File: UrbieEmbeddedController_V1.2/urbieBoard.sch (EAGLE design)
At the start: 81 parts, among them IC1 IC_FT311D-LQFP-32, J1 DURACLIK-4SMD, Q1 PFET, Q2 2N3904, U2 MAX232TSSOP, Y3 12mHz

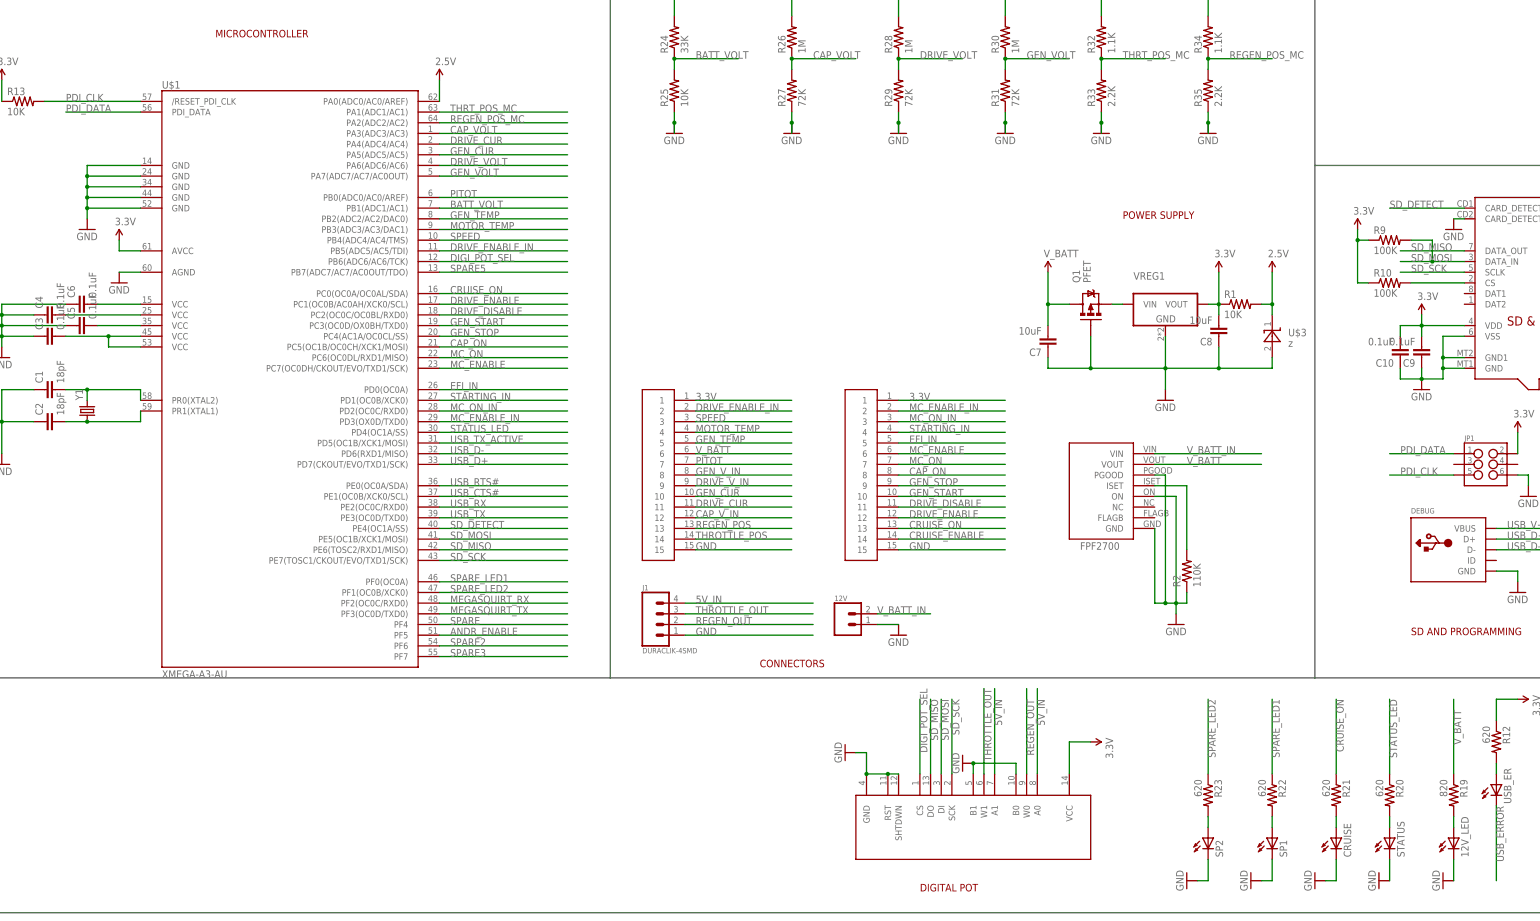
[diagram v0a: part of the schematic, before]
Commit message: Additions to Version 1.2
Added the 12V to 5V regulator circuit
Fixed SPI SS lines
Added SPI Header
Added TWI Header
Added Silkscreen
TODO: Adjust voltage divider values to get max 2.5V for ADCs
TODO: Pull TWI lines to high
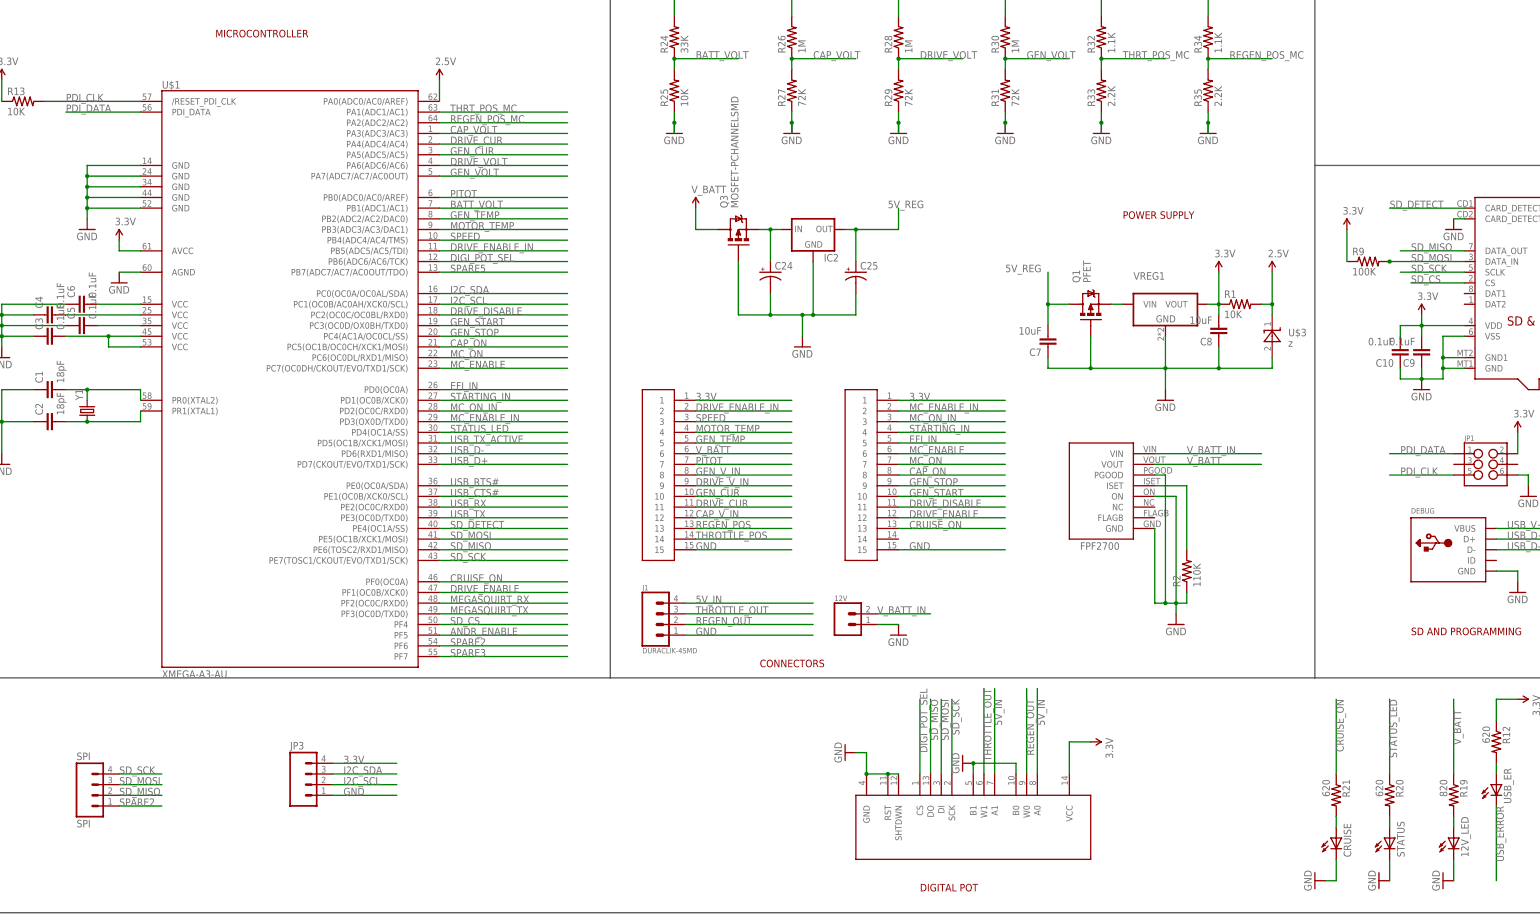
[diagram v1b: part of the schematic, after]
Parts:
- removed R10: 100K, SparkFun-Passives:RESISTOR0603-RES
- removed R22, R23: 620, SparkFun-Passives:RESISTOR0603-RES
- removed SP1, SP2: (no value), adafruit:LEDCHIP-LED0603
- added C24, C25: (no value), SparkFun-Passives:CAP_POLPTH2
- added IC2: (no value), SparkFun-PowerIC:V_REG_78XXSINK
- added JP3: (no value), SparkFun-Connectors:M04POLAR_LOCK
- added Q3: MOSFET-PCHANNELSMD, SparkFun-DiscreteSemi:MOSFET-PCHANNELSMD
- added SPI: SPI, SparkFun-Connectors:M04POLAR_LOCK
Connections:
- removed net CRUISE_ENABLE: U$9.14
- removed net N$17: R10.2, U$2.CS
- removed net N$32: R22.2, SP1.A
- removed net N$34: R23.2, SP2.A
- removed net SPARE: U$1.PF4
- removed net SPARE_LED1: R22.1, U$1.PF0(OC0A)
- removed net SPARE_LED2: R23.1, U$1.PF1(OC0B/XCK0)
- new net 5V_REG: C25.+, C7.2, IC2.OUT, Q1.D
- new net I2C_SCL: JP3.2, U$1.PC1(OC0B/AC0AH/XCK0/SCL)
- new net I2C_SDA: JP3.3, U$1.PC0(OC0A/OC0AL/SDA)
- new net N$14: C24.+, IC2.IN, Q3.S
- new net SD_CS: U$1.PF4, U$2.CS
- net 3.3V: now also JP3.4; no longer R10.1
- net CRUISE_ON: now also U$1.PF0(OC0A); no longer U$1.PC0(OC0A/OC0AL/SDA)
- net DRIVE_ENABLE: now also U$1.PF1(OC0B/XCK0); no longer U$1.PC1(OC0B/AC0AH/XCK0/SCL)
- net GND: now also C24.-, C25.-, IC2.GND, JP3.1, Q3.G; no longer SP1.C, SP2.C
- net SD_MISO: now also SPI.2
- net SD_MOSI: now also SPI.3
- net SD_SCK: now also SPI.4
- net SPARE2: now also SPI.1
- net V_BATT: now also Q3.D; no longer C7.2, Q1.D
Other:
- moved on the sheet: R9

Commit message: Fixed ADC values and pin routing
Fixed the voltage divider values to output 2.5V max signal voltage for
ADC
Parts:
- R25: value 10K -> 7.5K
- R27, R29, R31: value 72K -> 51K
- R33, R35: value 2.2K -> 1.0K
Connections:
- removed net 5V_IN: DIGI_POT.A0, DIGI_POT.A1, J1.PIN4
- net 5V_REG: now also DIGI_POT.A0, DIGI_POT.A1, J1.PIN4
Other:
- note added: "LED'S"
- moved on the sheet: 12V, 12V_LED, ANDROID, C1, C10, C11, C12, C13, C14, C15, C16, C17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

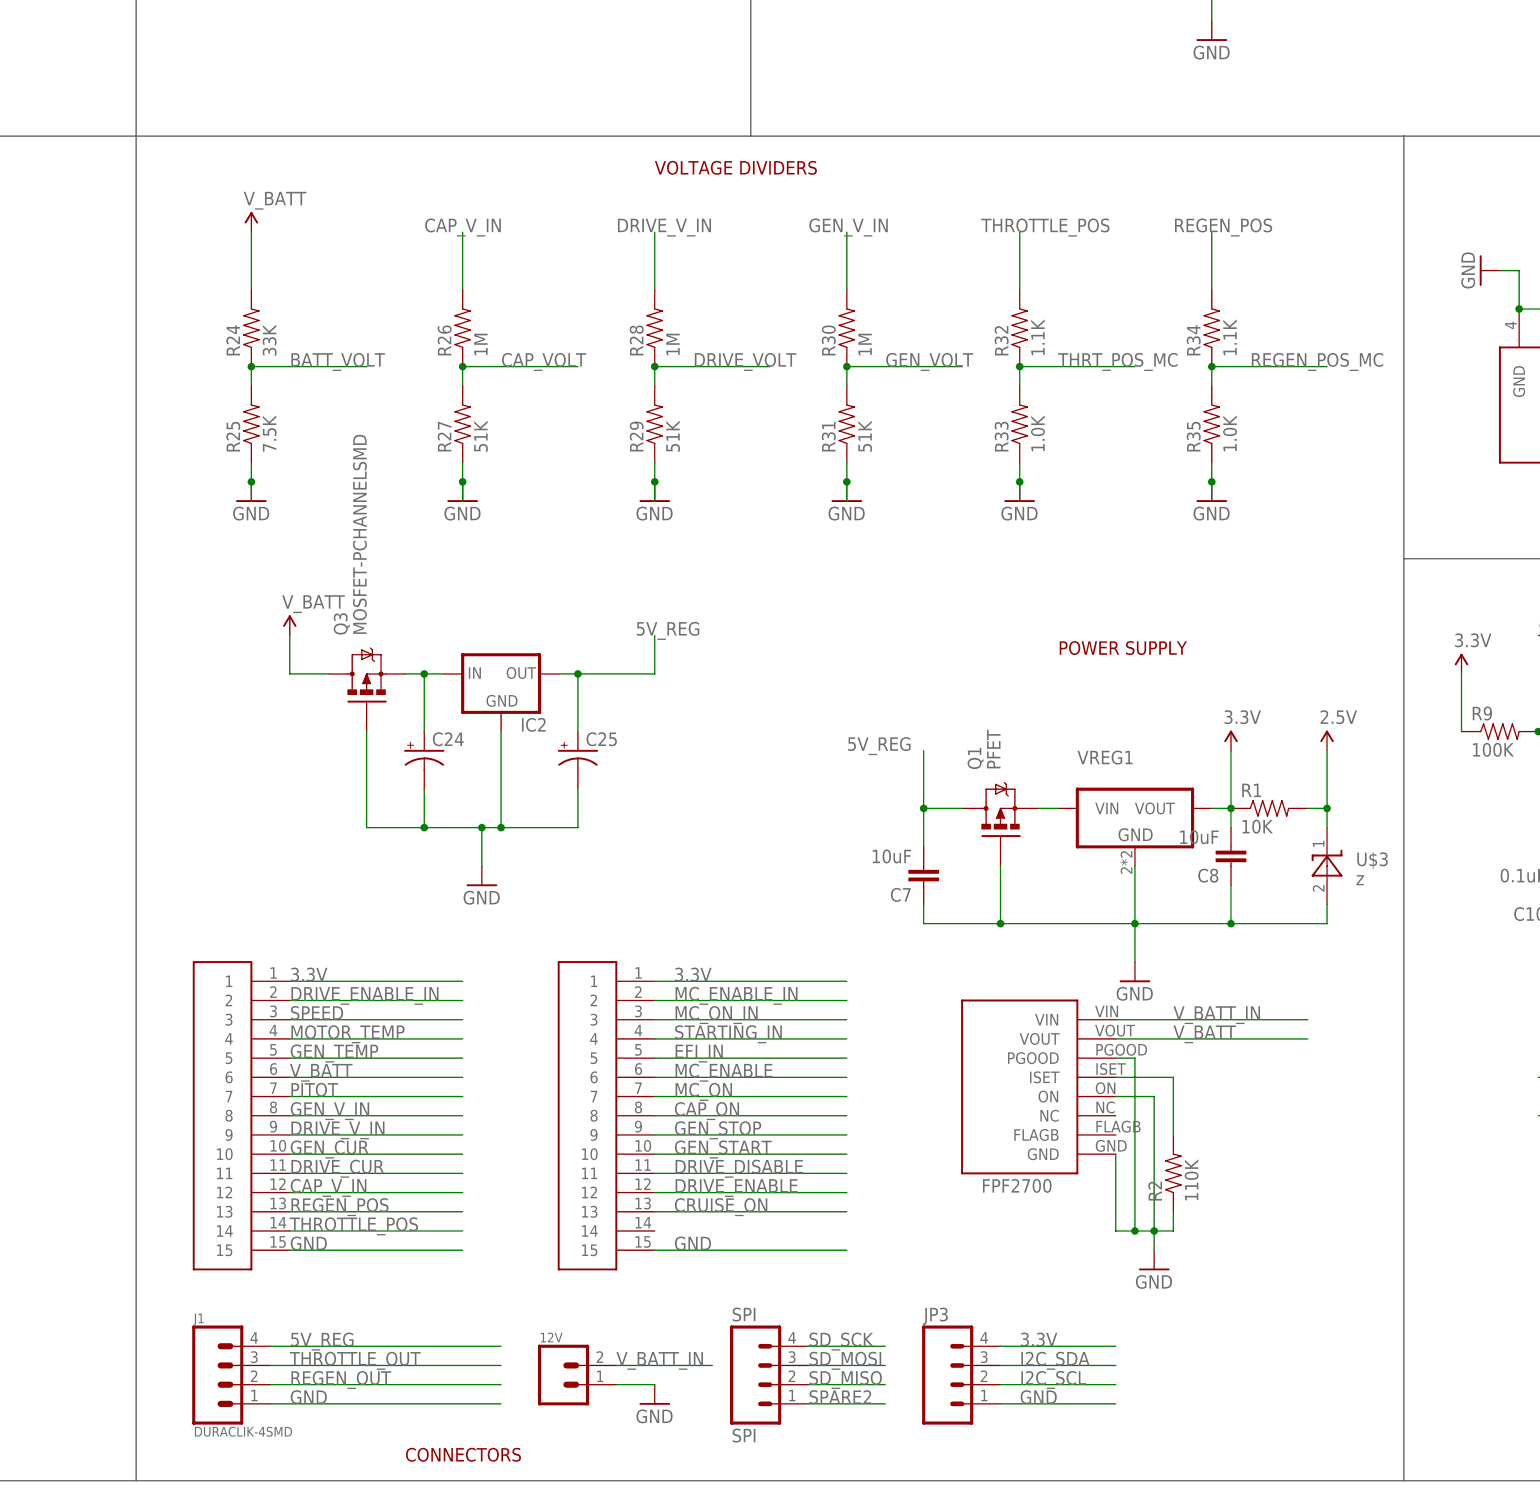
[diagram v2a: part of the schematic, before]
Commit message: small aesthetic fixes
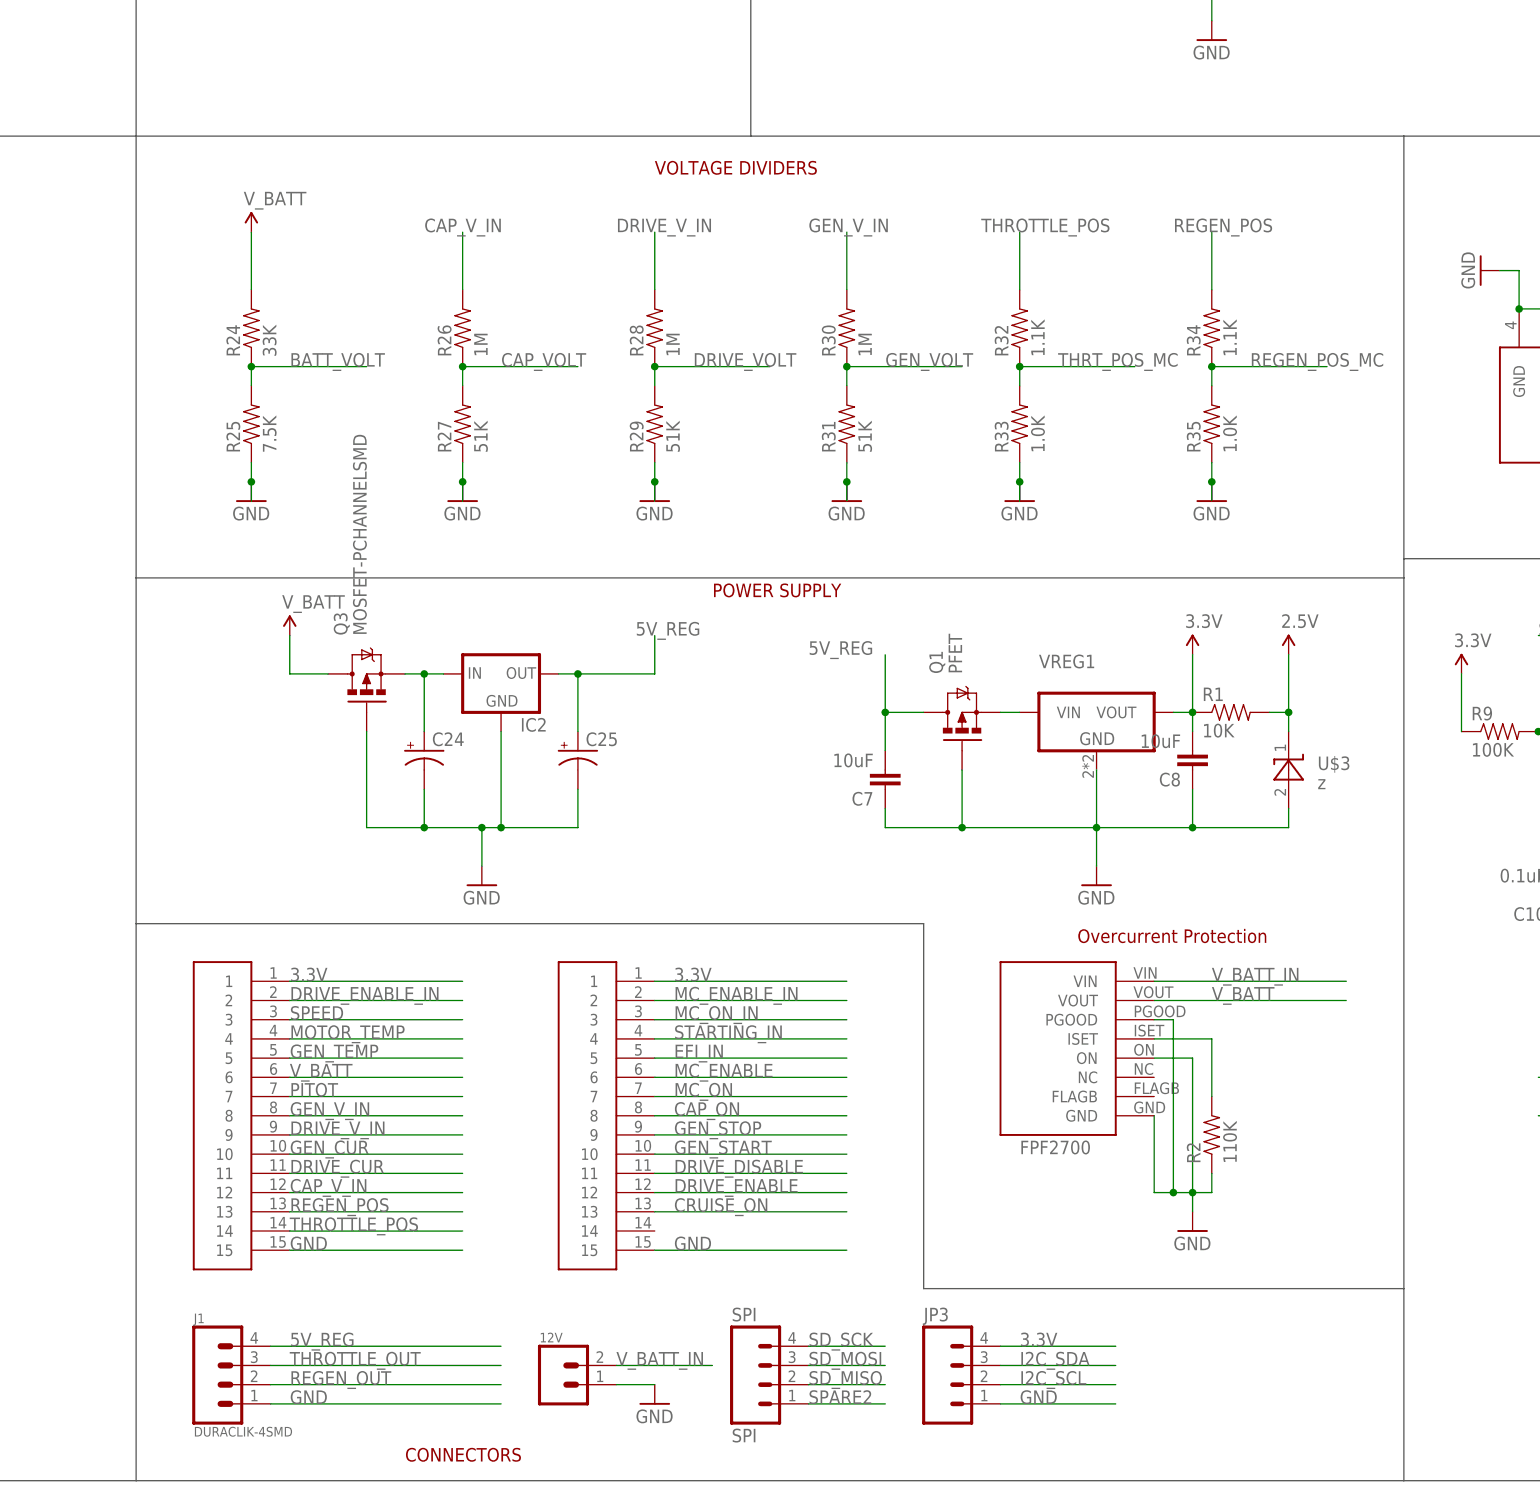
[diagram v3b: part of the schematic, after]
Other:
- note added: "Overcurrent Protection"
- moved on the sheet: C7, C8, Q1, R1, R2, U$3, VREG1

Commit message: Gerbers and connector changes
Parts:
- removed ANDROID: (no value), adafruit:USBMINIB
- removed DIGI_POT: MCP42XXX, SparkFun-AnalogIC:MCP42XXX
- removed J1: DURACLIK-4SMD, Senior Design:DURACLIK-4SMD
- removed Q1: PFET, SparkFun-DiscreteSemi:MOSFET-PCHANNELSMD
- removed Q3: MOSFET-PCHANNELSMD, SparkFun-DiscreteSemi:MOSFET-PCHANNELSMD
- removed U$7, U$9: MOLEX15_PIN, Molex15_pin:MOLEX15_PIN
- added JP2: (no value), jumper:JP1E
- added JP4: USB-A-S, SparkFun-Connectors:USB-A-S
- added U$10, U$11: 15PIN, 15pinconn:15PIN
- 12V, 12V_LED, C10, C11, C12, C13, C14, C15, C16, C17, C18, C19, C20, C21, C3, C4, C5, C6, C7, C8, C9, CRUISE, DEBUG, IC1, IC2, JP1, JP3, L1, LOGO1, PCB1, R1, R11, R12, R13, R14, R15, R16, R17, R18, R19, R2, R20, R21, R24, R25, R26, R27, R28, R29, R30, R31, R32, R33, R34, R35, R9, SPI, STATUS, U$1, U$2, U$3, U$8, U2, USB_ER, VREG1, X1, Y1, Y3: OC_NEWARK (none) -> unknown
- C1, C2, C22, C23: MPN (none) -> 06031A180JAT2A; OC_NEWARK (none) -> 60R6182
- C24, C25: value (none) -> 4.7uF; OC_NEWARK (none) -> unknown
- Q2: value 2N3904 -> MMBT3904; device SparkFun-DiscreteSemi:TRANSISTOR_NPNSOT23 -> transistor-npn:BCX20SMD; OC_NEWARK (none) -> unknown
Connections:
- removed net N$14: C24.+, IC2.IN, Q3.S
- removed net N$3: Q1.S, VREG1.VIN
- removed net N$4: C6.2, U$1.VCC1
- removed net N$5: C4.2, U$1.VCC2
- removed net N$6: C5.2, U$1.VCC3
- removed net N$7: C3.2, U$1.VCC4, U$1.VCC5
- removed net REGEN_OUT: DIGI_POT.W0, J1.PIN2
- removed net THROTTLE_OUT: DIGI_POT.W1, J1.PIN3
- net 3.3V: now also C3.2, C4.2, C5.2, C6.2, U$1.VCC1, U$1.VCC2, U$1.VCC3, U$1.VCC4, U$1.VCC5, U$10.PIN1, U$11.PIN1; no longer DIGI_POT.VCC, U$7.1, U$9.1
- net 5V_REG: now also VREG1.VIN; no longer DIGI_POT.A0, DIGI_POT.A1, J1.PIN4, Q1.D
- net ANDROID_D+: now also JP4.D+; no longer ANDROID.D+
- net ANDROID_D-: now also JP4.D-; no longer ANDROID.D-
- net CAP_ON: now also U$11.PIN8; no longer U$9.8
- net CAP_V_IN: now also U$10.PIN12; no longer U$7.12
- net CRUISE_ON: now also U$11.PIN13; no longer U$9.13
- net DIGI_POT_SEL: no longer DIGI_POT.CS
- net DRIVE_CUR: now also U$10.PIN11; no longer U$7.11
- net DRIVE_DISABLE: now also U$11.PIN11; no longer U$9.11
- net DRIVE_ENABLE: now also U$11.PIN12; no longer U$9.12
- net DRIVE_ENABLE_IN: now also U$10.PIN2; no longer U$7.2
- net DRIVE_V_IN: now also U$10.PIN9; no longer U$7.9
- net EFI_IN: now also U$11.PIN5; no longer U$9.5
- net GEN_CUR: now also U$10.PIN10; no longer U$7.10
- net GEN_START: now also U$11.PIN10; no longer U$9.10
- net GEN_STOP: now also U$11.PIN9; no longer U$9.9
- net GEN_TEMP: now also U$10.PIN5; no longer U$7.5
- net GEN_V_IN: now also U$10.PIN8; no longer U$7.8
- net GND: now also JP4.GND, U$10.PIN15, U$11.PIN15; no longer ANDROID.GND, DIGI_POT.B0, DIGI_POT.B1, DIGI_POT.GND, DIGI_POT.RST, DIGI_POT.SHTDWN, J1.PIN1, Q1.G, Q3.G, U$7.15, U$9.15
- net MC_ENABLE: now also U$11.PIN6; no longer U$9.6
- net MC_ENABLE_IN: now also U$11.PIN2; no longer U$9.2
- net MC_ON: now also U$11.PIN7; no longer U$9.7
- net MC_ON_IN: now also U$11.PIN3; no longer U$9.3
- net MOTOR_TEMP: now also U$10.PIN4; no longer U$7.4
- net N$24: now also JP4.VBUS; no longer ANDROID.VBUS
- net PITOT: now also U$10.PIN7; no longer U$7.7
- net REGEN_POS: now also U$10.PIN13; no longer U$7.13
- net SD_MISO: no longer DIGI_POT.DO
- net SD_MOSI: no longer DIGI_POT.DI
- net SD_SCK: no longer DIGI_POT.SCK
- net SPEED: now also U$10.PIN3; no longer U$7.3
- net STARTING_IN: now also U$11.PIN4; no longer U$9.4
- net THROTTLE_POS: now also U$10.PIN14; no longer U$7.14
- net V_BATT: now also C24.+, IC2.IN, JP2.1, U$10.PIN6; no longer Q3.D, U$7.6
- net V_BATT_IN: now also JP2.2
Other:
- moved on the sheet: C24, C25, C7, L1
